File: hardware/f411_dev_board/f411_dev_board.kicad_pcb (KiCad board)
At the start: 2 copper layers, 33 parts, among them J1 Conn_01x15, J2 Conn_01x15, J3 Conn_01x04, J4 USB_C_Receptacle_USB2.0_16P, SW1 SW_SPDT, SW2 SW_Push, U1 STM32F411CEU6, U2 USBLC6-2SC6, U3 AMS1117-3.3, Y1 24MHz

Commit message: finished pcb layout v1
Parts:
- C1, C11, C12, C2, C3, C4, C5, C9, R1, R2, U3: moved to B.Cu
- moved J4 109.8 mm to (192.3, 86.4), turned to 90 degrees
- moved C11 104.5 mm to (183.1, 91.0)
- moved C12 103.2 mm to (182.1, 82.2)
- moved D2 98.9 mm to (194.6, 93.5), turned to -90 degrees
- moved D1 98.3 mm to (194.1, 79.0), turned to -90 degrees
- moved U2 97.8 mm to (184.2, 88.6)
- moved C10 96.5 mm to (178.8, 83.3), turned to 90 degrees
- moved R1 96.1 mm to (193.3, 88.9), turned to -90 degrees
- moved C5 95.7 mm to (173.4, 88.0), turned to 90 degrees
- moved R2 95.3 mm to (193.3, 85.1), turned to -90 degrees
- moved R7 95.1 mm to (193.0, 93.5), turned to -90 degrees
- moved R6 94.7 mm to (193.3, 80.5)
- moved C9 93.6 mm to (171.7, 92.3)
- moved SW2 91.9 mm to (183.1, 83.3)
- moved C4 90.6 mm to (172.8, 82.7), turned to -90 degrees
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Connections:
- U2 pad 1: USB_CONN_D- -> USB_D+
- U2 pad 3: USB_CONN_D+ -> USB_D-
- U2 pad 4: USB_D+ -> USB_CONN_D-
- U2 pad 6: USB_D- -> USB_CONN_D+
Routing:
- net +3V3: track 0.00 -> 121.9 mm, vias 0 -> 7
- net VBUS: track 0.00 -> 84.2 mm, vias 0 -> 3
- net BUILTIN_LED: track 0.00 -> 81.1 mm, vias 0 -> 2
- net PA8: track 0.00 -> 75.1 mm, vias 0 -> 2
- net SWDIO: track 0.00 -> 51.8 mm, vias 0 -> 4
- net SWCLK: track 0.00 -> 45.6 mm
- net GND: track 0.00 -> 45.0 mm, vias 0 -> 9
- net PB12: track 0.00 -> 42.7 mm, vias 0 -> 4
- net PA9: track 0.00 -> 42.0 mm, vias 0 -> 1
- net PA10: track 0.00 -> 35.6 mm, vias 0 -> 2
- net RESET: track 0.00 -> 27.3 mm, vias 0 -> 4
- net PA0: track 0.00 -> 18.3 mm
- net PA1: track 0.00 -> 15.6 mm
- net BOOT0: track 0.00 -> 14.3 mm, vias 0 -> 2
- net USB_D-: track 0.00 -> 14.1 mm
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- added copper zone on B.Cu, net +3V3
- added copper zone on B.Cu, net GND
- added copper zone on F.Cu, net VBUS
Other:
- board outline added: 52.8 x 20.3 mm

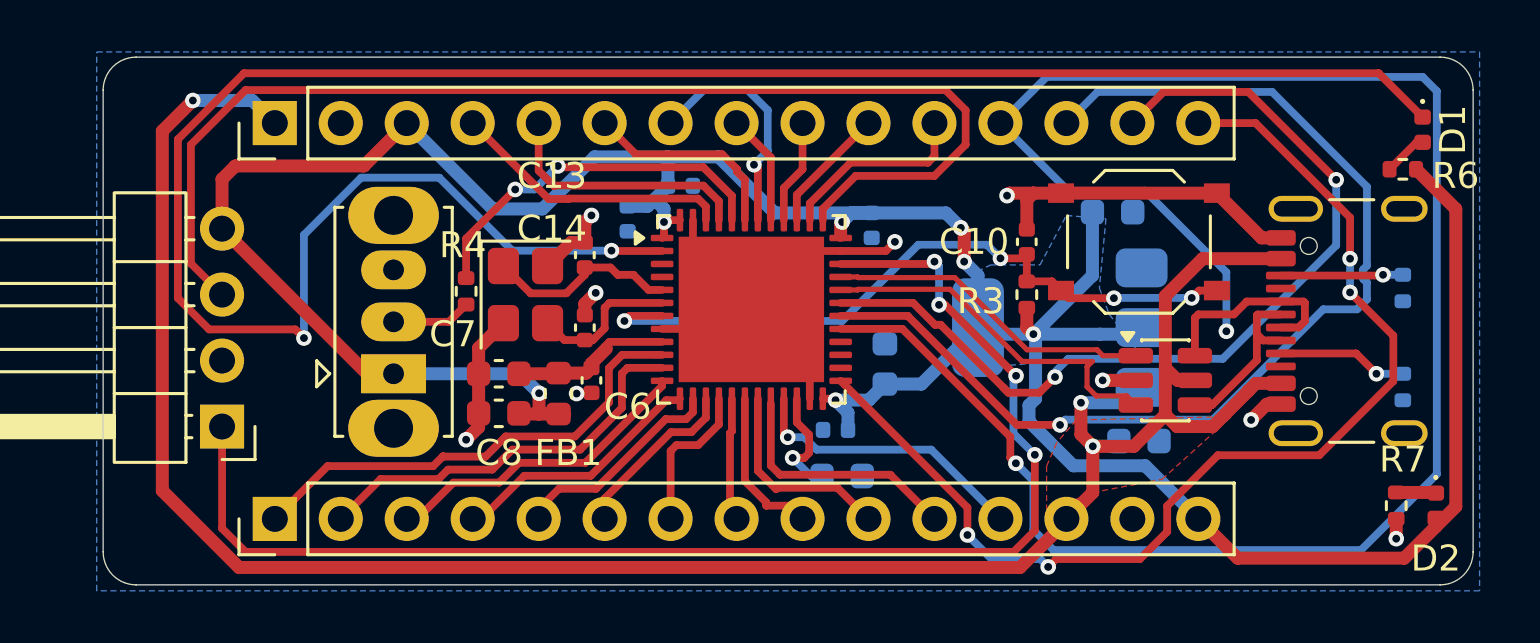
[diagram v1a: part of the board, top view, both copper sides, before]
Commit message: finish pcb v2
also reorganized schematic
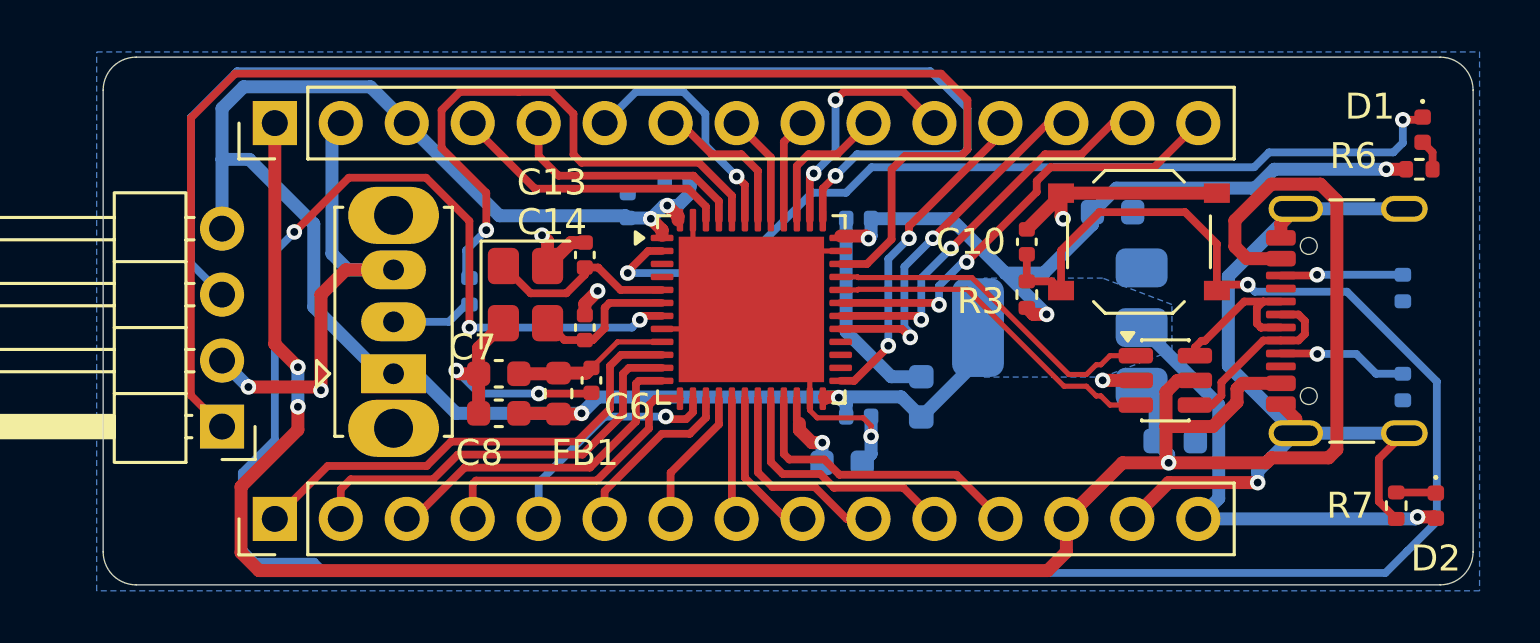
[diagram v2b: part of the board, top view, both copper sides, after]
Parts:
- R4: moved to B.Cu
- moved C5 1.89 mm to (174.8, 89.3)
- moved C11 1.40 mm to (184.5, 91.0)
- moved C3 1.03 mm to (172.3, 90.0), turned to 0 degrees
- moved R6 0.63 mm to (193.9, 80.5), turned to 180 degrees
- moved C4 0.57 mm to (172.3, 82.4), turned to 180 degrees
- moved C2 0.51 mm to (163.4, 81.9), turned to 90 degrees
- moved C9 0.51 mm to (171.7, 91.8)
- moved C1 0.18 mm to (165.4, 81.0), turned to 180 degrees
- moved R4 0.13 mm to (157.4, 85.2)
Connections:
- J2 pad 12: PA8 -> PB12
- J2 pad 13: PA9 -> PA8
- J2 pad 14: PA10 -> PA9
- J2 pad 15: PB12 -> PA10
- J4 pad SH: unconnected-(J4-SHIELD-PadSH)_3 -> GND
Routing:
- net RESET: track 27.3 -> 108.7 mm
- net GND: track 45.0 -> 107.8 mm, vias 9 -> 10
- net PA8: track 75.1 -> 14.2 mm
- net BUILTIN_LED: track 81.1 -> 35.3 mm
- net PB12: track 42.7 -> 12.8 mm, vias 4 -> 2
- net PA9: track 42.0 -> 15.4 mm, vias 1 -> 2
- net PA10: track 35.6 -> 17.4 mm
- net VBUS: track 84.2 -> 93.1 mm
- net BOOT0: track 14.3 -> 22.5 mm, vias 2 -> 1
- net +3V3: track 121.9 -> 115.6 mm, vias 7 -> 8
- net PB6: track 9.10 -> 6.02 mm, vias 1 -> 0
- net PA15: track 7.47 -> 9.47 mm, vias 0 -> 2
- net SWCLK: track 45.6 -> 47.5 mm, vias 0 -> 1
- net SWDIO: track 51.8 -> 53.6 mm, vias 4 -> 0
- net PB7: track 7.92 -> 9.45 mm, vias 0 -> 1
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- removed copper zone on F.Cu, net VBUS
